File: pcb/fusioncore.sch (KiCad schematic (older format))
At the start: 114 parts, among them J1 Conn_02x12_Top_Bottom, J10 Pump_Misc_1, J11 Pump_Misc_2, J12 Flow_Warm, J13 Flow_Cold, J14 Trigger, J15 Valve_M2, J16 Valve_M3, J17 Valve_M4, J18 Conn_02x03_Top_Bottom, J19 Valve_Air_Lime, J2 Temperature, J20 Valve_Air_Rum, J21 Valve_Air_Out, J22 LED, J23 I2C_DBG, J3 40HAT, J4 Valve_M1, J5 WEIGHT, J6 Pump_Cold, J7 Pump_Warm, J8 Pump_Air, J9 CONN_01X02, Q1 DMG2305UX, Q12 AO3400A, Q13 AO3400A, Q14 AO3400A, Q16 MMBT4403, Q2 DMMT5401, Q3 AO3400A, Q4 AO3400A, Q5 AO3400A, Q6 AO3400A, Q7 AO3400A, SW1 POWER_ON, U1 HX711, U2 CAT24C32, U3 LTC2990, U4 LTC2990, U5 TXB0108DQSR

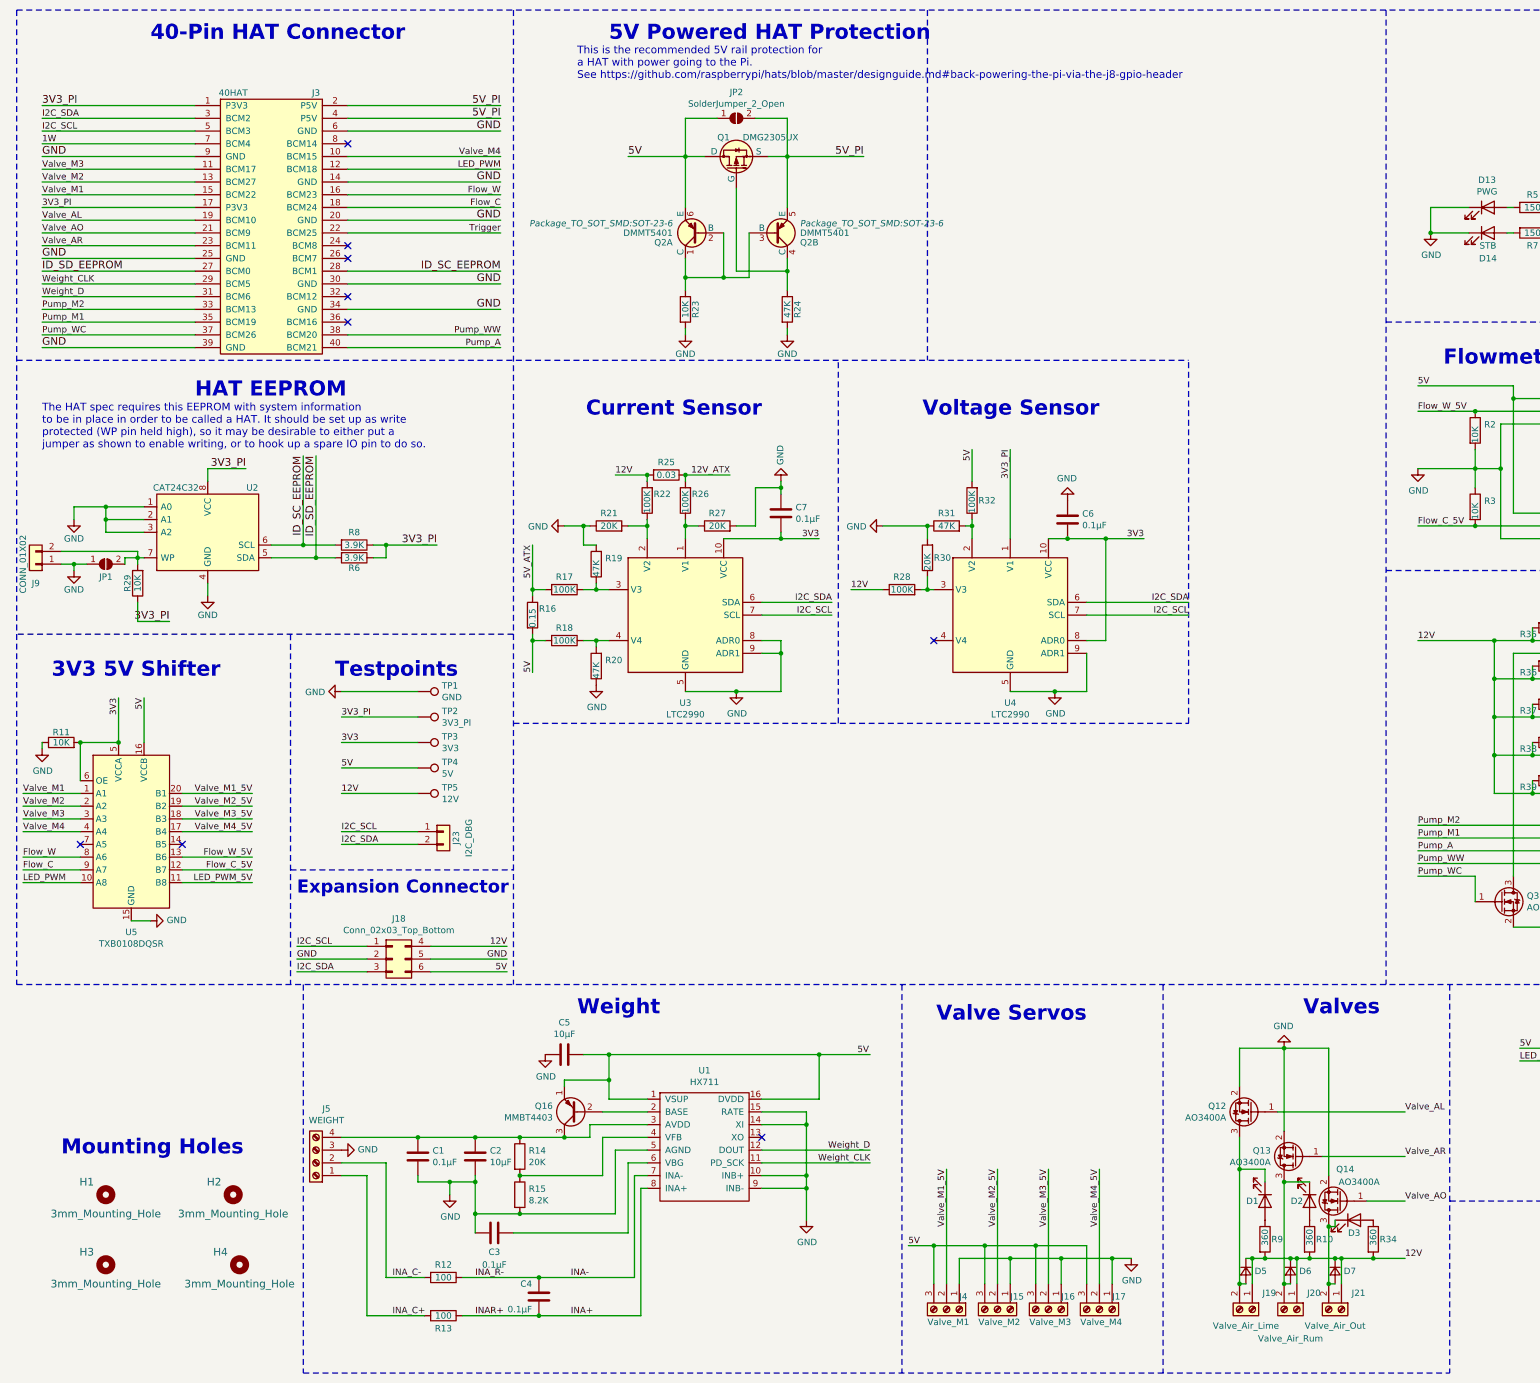
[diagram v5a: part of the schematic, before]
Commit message: Added JLC specific marker
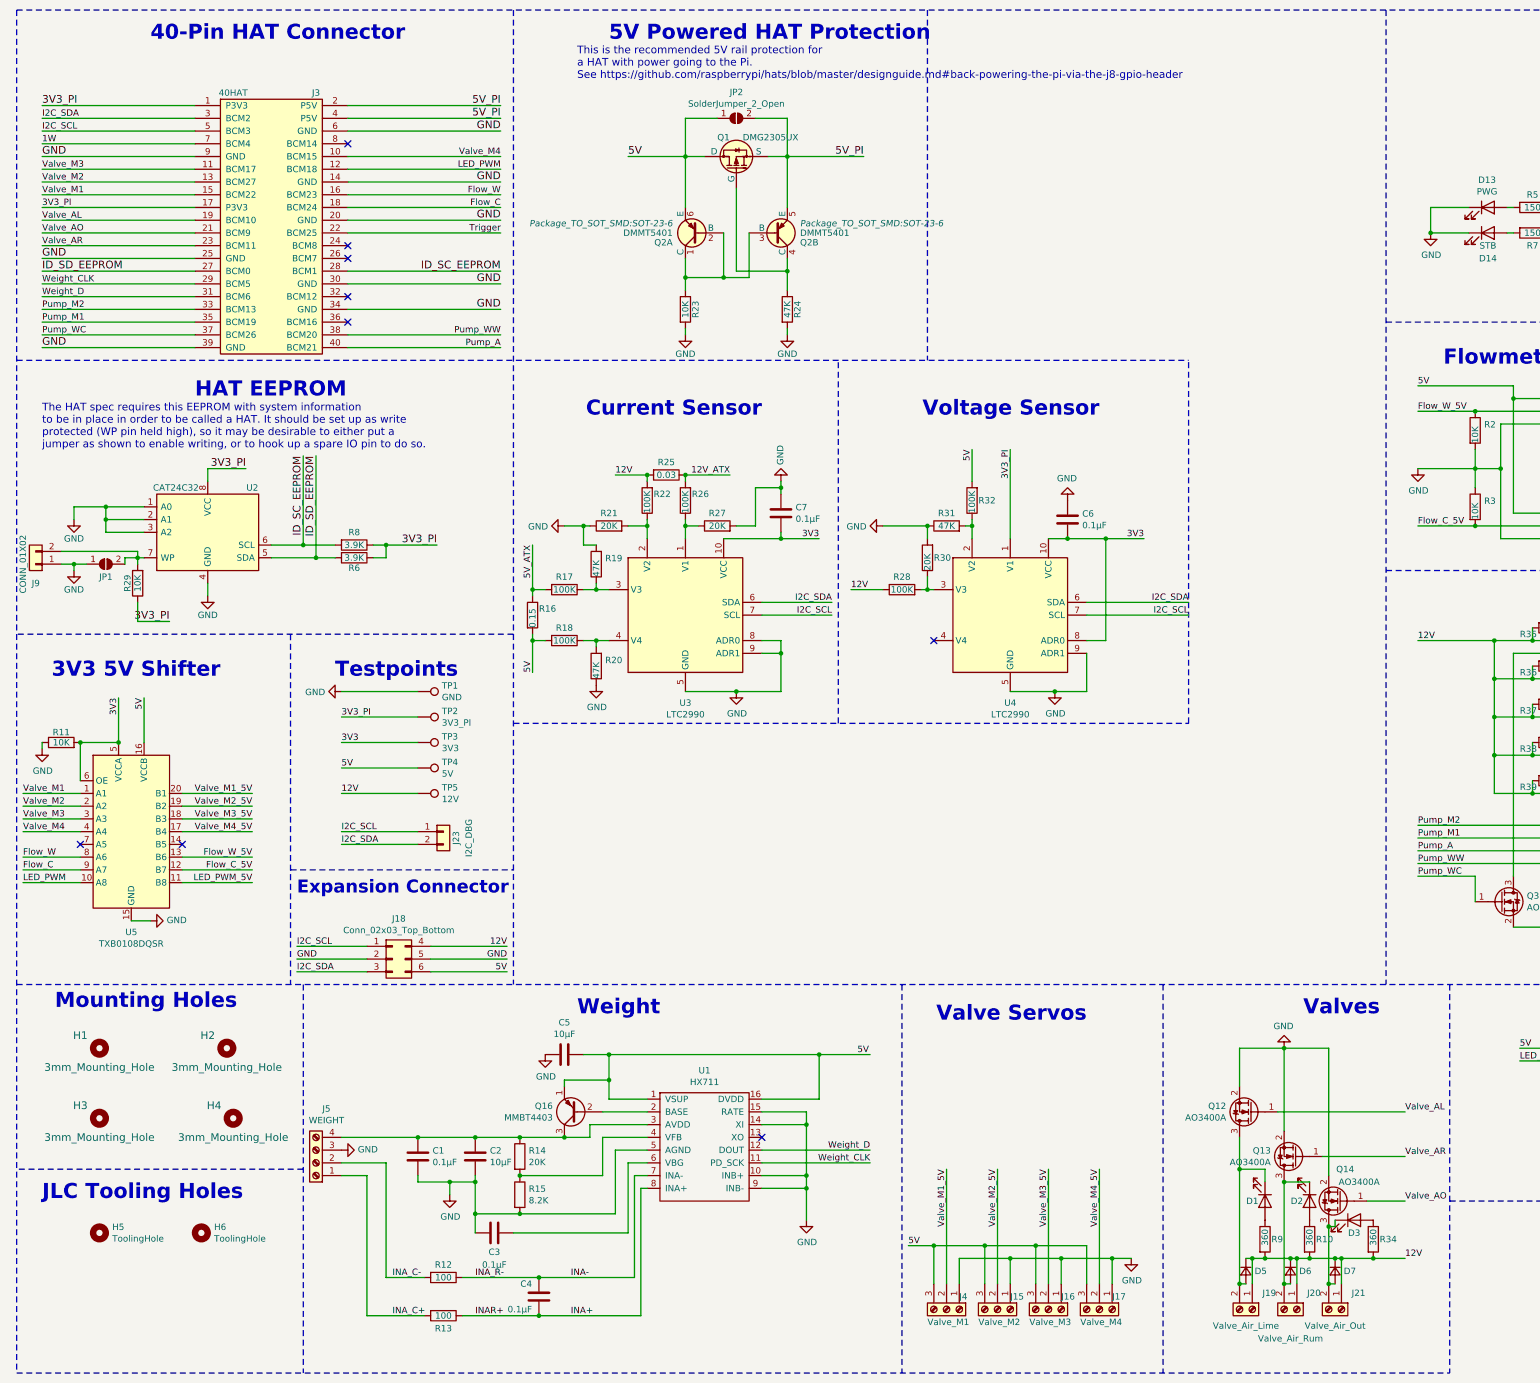
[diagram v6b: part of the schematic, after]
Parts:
- added H5, H6: ToolingHole, project_footprints:JLC_Tooling_Hole, symbol Mechanical:MountingHole
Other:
- note added: "JLC Tooling Holes"
- moved on the sheet: H1, H2, H3, H4
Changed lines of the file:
@@
 L Mechanical:MountingHole H1
 U 1 1 5834BC4A
-P 1200 9800
-F 0 "H1" H 1050 9900 60  0000 C CNN
-F 1 "3mm_Mounting_Hole" H 1200 9650 60  0000 C CNN
-F 2 "project_footprints:NPTH_3mm_ID" H 1100 9800 60  0001 C CNN
-F 3 "" H 1100 9800 60  0001 C CNN
-	1    1200 9800
+P 1150 8650
+F 0 "H1" H 1000 8750 60  0000 C CNN
+F 1 "3mm_Mounting_Hole" H 1150 8500 60  0000 C CNN
+F 2 "project_footprints:NPTH_3mm_ID" H 1050 8650 60  0001 C CNN
+F 3 "" H 1050 8650 60  0001 C CNN
+	1    1150 8650
 	1    0    0    -1
 $EndComp
@@
 L Mechanical:MountingHole H2
 U 1 1 5834BCDF
-P 2200 9800
-F 0 "H2" H 2050 9900 60  0000 C CNN
-F 1 "3mm_Mounting_Hole" H 2200 9650 60  0000 C CNN
-F 2 "project_footprints:NPTH_3mm_ID" H 2100 9800 60  0001 C CNN
-F 3 "" H 2100 9800 60  0001 C CNN
-	1    2200 9800
+P 2150 8650
+F 0 "H2" H 2000 8750 60  0000 C CNN
+F 1 "3mm_Mounting_Hole" H 2150 8500 60  0000 C CNN
+F 2 "project_footprints:NPTH_3mm_ID" H 2050 8650 60  0001 C CNN
+F 3 "" H 2050 8650 60  0001 C CNN
+	1    2150 8650
 	1    0    0    -1
 $EndComp
@@
 L Mechanical:MountingHole H3
 U 1 1 5834BD62
-P 1200 10350
-F 0 "H3" H 1050 10450 60  0000 C CNN
-F 1 "3mm_Mounting_Hole" H 1200 10200 60  0000 C CNN
-F 2 "project_footprints:NPTH_3mm_ID" H 1100 10350 60  0001 C CNN
-F 3 "" H 1100 10350 60  0001 C CNN
-	1    1200 10350
+P 1150 9200
+F 0 "H3" H 1000 9300 60  0000 C CNN
+F 1 "3mm_Mounting_Hole" H 1150 9050 60  0000 C CNN
+F 2 "project_footprints:NPTH_3mm_ID" H 1050 9200 60  0001 C CNN
+F 3 "" H 1050 9200 60  0001 C CNN
+	1    1150 9200
 	1    0    0    -1
 $EndComp
@@
 L Mechanical:MountingHole H4
 U 1 1 5834BDED
-P 2250 10350
-F 0 "H4" H 2100 10450 60  0000 C CNN
-F 1 "3mm_Mounting_Hole" H 2250 10200 60  0000 C CNN
-F 2 "project_footprints:NPTH_3mm_ID" H 2150 10350 60  0001 C CNN
-F 3 "" H 2150 10350 60  0001 C CNN
-	1    2250 10350
+P 2200 9200
+F 0 "H4" H 2050 9300 60  0000 C CNN
+F 1 "3mm_Mounting_Hole" H 2200 9050 60  0000 C CNN
+F 2 "project_footprints:NPTH_3mm_ID" H 2100 9200 60  0001 C CNN
+F 3 "" H 2100 9200 60  0001 C CNN
+	1    2200 9200
 	1    0    0    -1
 $EndComp
@@
 Text Notes 1900 3550 0    118  ~ 24
 HAT EEPROM
-Text Notes 850  9500 0    118  ~ 24
+Text Notes 800  8350 0    118  ~ 24
 Mounting Holes
 Text Notes 1550 750  0    118  ~ 24
@@
 	2750 8150 2750 11200
 Wire Notes Line
-	2750 11200 11750 11200
-Wire Notes Line
 	13650 2950 13650 4900
 Wire Notes Line
@@
 	500  8150 16050 8150
 Wire Notes Line
-	500  500  500  8150
-Wire Notes Line
 	500  500  16050 500
 Text Notes 9000 3700 2    118  ~ 24
@@
 Text Label 3050 7050 0    50   ~ 0
 I2C_SDA
+Wire Notes Line
+	500  11200 11750 11200
+Wire Notes Line
+	500  500  500  11200
+Wire Notes Line
+	2750 9600 500  9600
+Text Notes 700  9850 0    118  ~ 24
+JLC Tooling Holes
+$Comp
+L Mechanical:MountingHole H5
+U 1 1 5E48D44C
+P 1150 10100
+F 0 "H5" H 1250 10146 50  0000 L CNN
+F 1 "ToolingHole" H 1250 10055 50  0000 L CNN
+F 2 "project_footprints:JLC_Tooling_Hole" H 1150 10100 50  0001 C CNN
+F 3 "~" H 1150 10100 50  0001 C CNN
+	1    1150 10100
+	1    0    0    -1
+$EndComp
+$Comp
+L Mechanical:MountingHole H6
+U 1 1 5E48DB8E
+P 1950 10100
+F 0 "H6" H 2050 10146 50  0000 L CNN
+F 1 "ToolingHole" H 2050 10055 50  0000 L CNN
+F 2 "project_footprints:JLC_Tooling_Hole" H 1950 10100 50  0001 C CNN
+F 3 "~" H 1950 10100 50  0001 C CNN
+	1    1950 10100
+	1    0    0    -1
+$EndComp
 $EndSCHEMATC

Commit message: Fix J23
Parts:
- J23: footprint Connector_PinHeader_2.54mm:PinHeader_1x02_P2.54mm_Vertical -> Connector_PinHeader_2.54mm:PinHeader_1x04_P2.54mm_Vertical; symbol Connector_Generic:Conn_01x02 -> Connector_Generic:Conn_01x04
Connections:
- net 3V3: now also J23.1 (Pin_1)
- net GND: now also J23.4 (Pin_4)
- net I2C_SCL: now also J23.2 (Pin_2); no longer J23.1 (Pin_1)
- net I2C_SDA: now also J23.3 (Pin_3); no longer J23.2 (Pin_2)
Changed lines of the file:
@@
 	3750 7850 4350 7850
 $Comp
-L Connector_Generic:Conn_01x02 J23
+L Connector_Generic:Conn_01x04 J23
 U 1 1 5E8D6410
 P 3850 6950
 F 0 "J23" V 3950 6900 50  0000 C CNN
 F 1 "I2C_DBG" V 4050 6900 50  0000 C CNN
-F 2 "Connector_PinHeader_2.54mm:PinHeader_1x02_P2.54mm_Vertical" H 3850 6950 50  0001 C CNN
+F 2 "Connector_PinHeader_2.54mm:PinHeader_1x04_P2.54mm_Vertical" H 3850 6950 50  0001 C CNN
 F 3 "" H 3850 6950 50  0000 C CNN
 	1    3850 6950
@@
 	1    0    0    -1
 $EndComp
+Wire Wire Line
+	3650 6850 3050 6850
+Wire Wire Line
+	3650 7150 3050 7150
+Text Label 3050 6850 0    50   ~ 0
+3V3
+Text Label 3050 7150 0    50   ~ 0
+GND
 $EndSCHEMATC

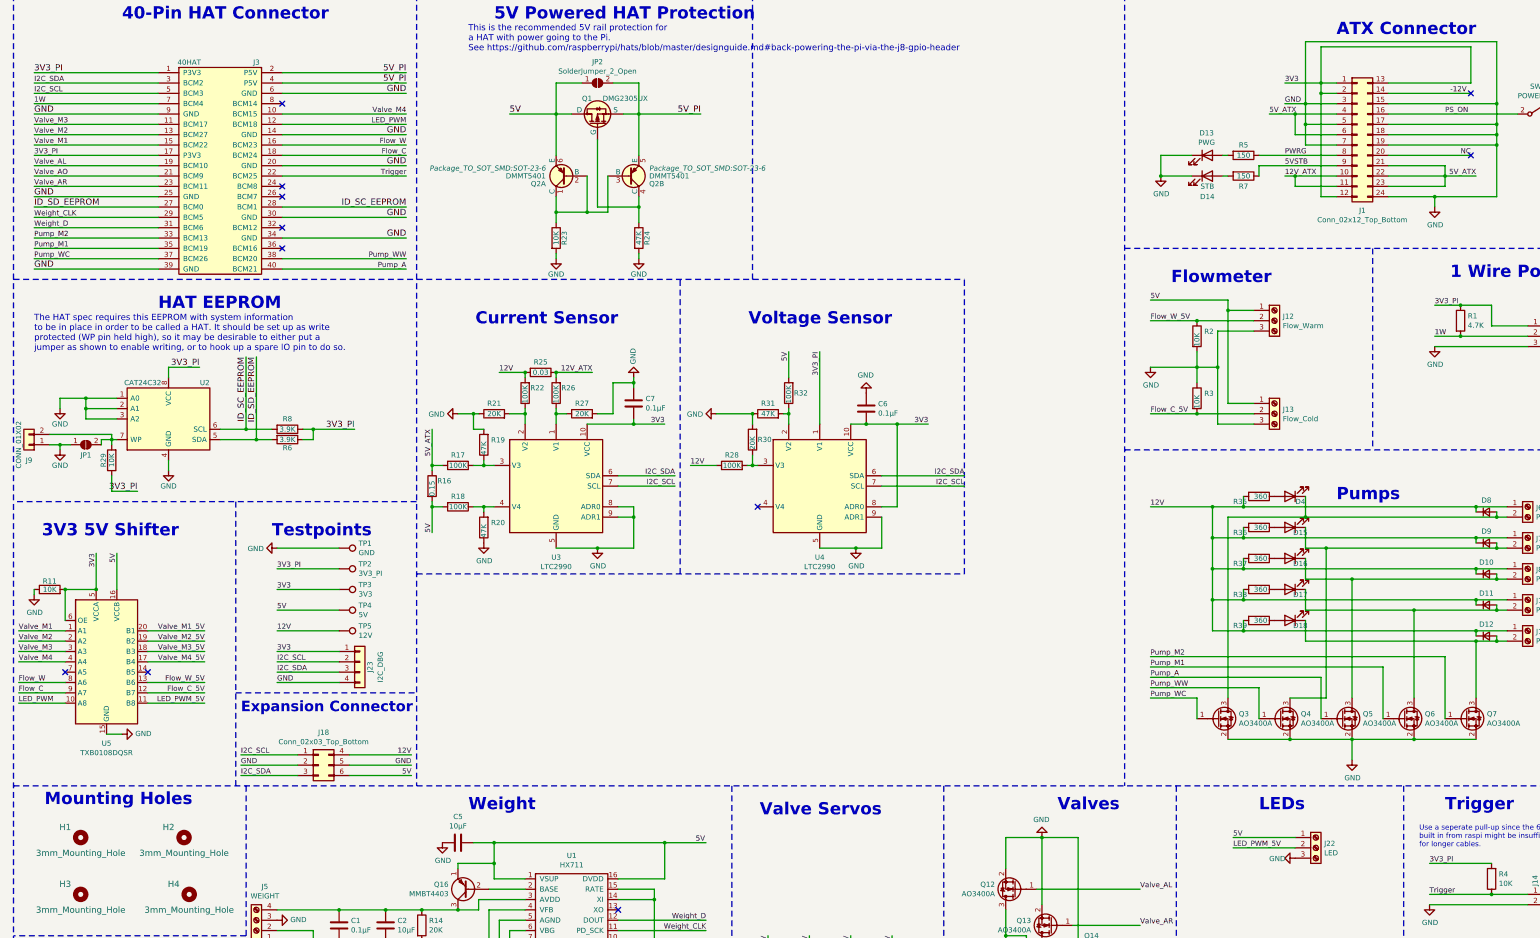
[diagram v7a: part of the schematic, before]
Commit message: Replaced LTC2990 with INA226 in schema
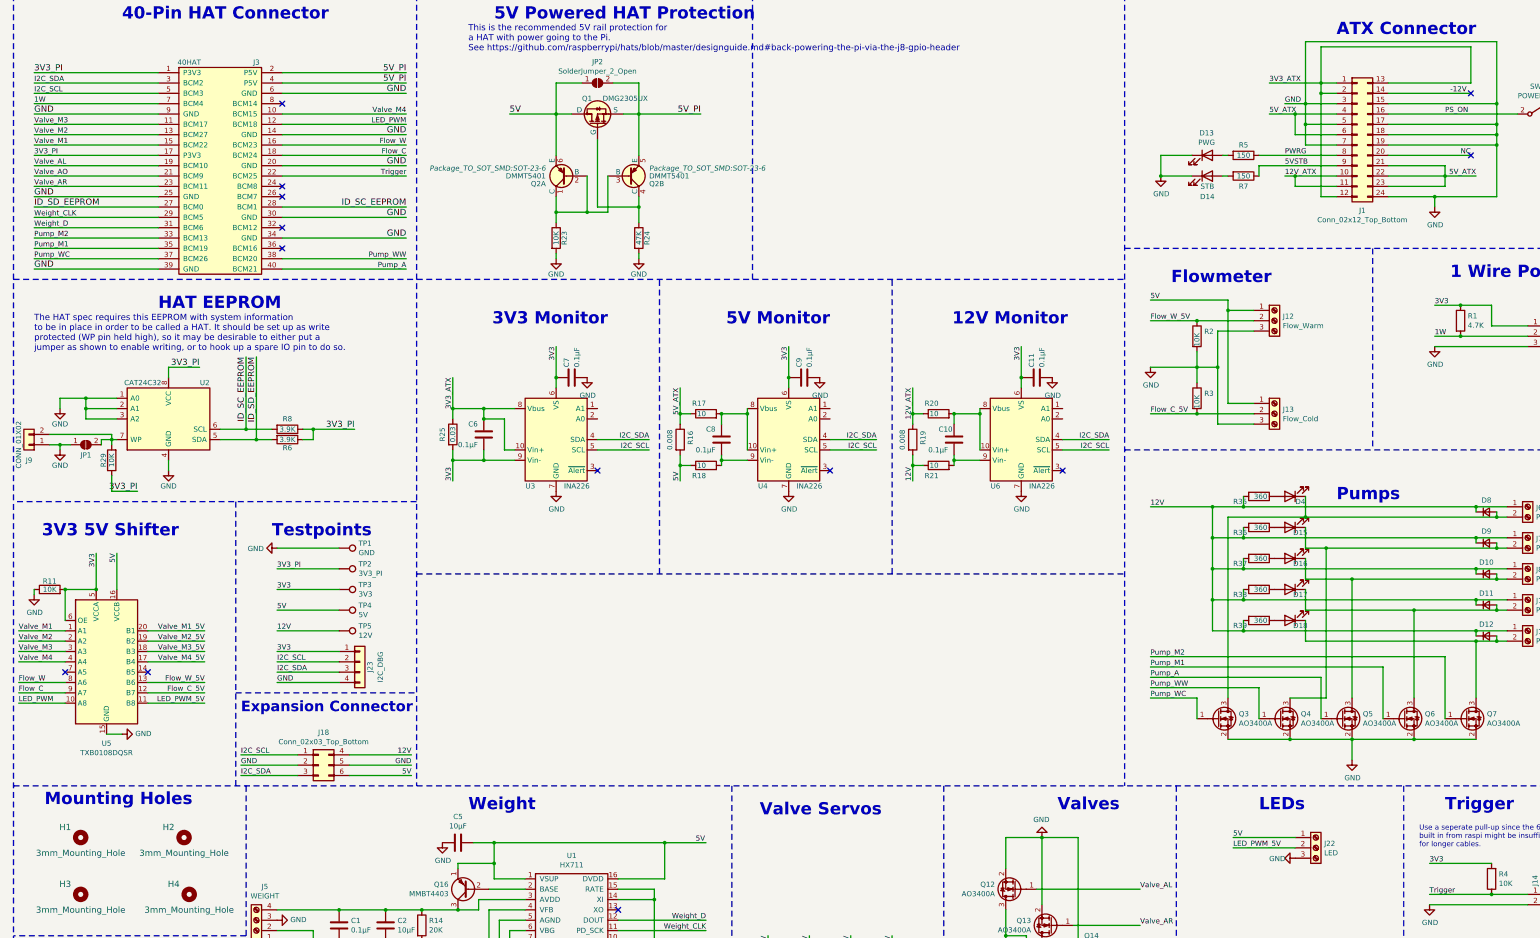
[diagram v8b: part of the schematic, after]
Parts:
- removed R22, R26, R28, R32: 100K, Resistor_SMD:R_0805_2012Metric_Pad1.15x1.40mm_HandSolder, symbol Device:R
- removed R27, R30: 20K, Resistor_SMD:R_0805_2012Metric_Pad1.15x1.40mm_HandSolder, symbol Device:R
- removed R31: 47K, Resistor_SMD:R_0805_2012Metric_Pad1.15x1.40mm_HandSolder, symbol Device:R
- removed U3, U4: LTC2990, Package_SO:MSOP-10_3x3mm_P0.5mm, symbol Sensor:LTC2990
- added C10, C11, C8, C9: 0.1μF, Capacitor_SMD:C_0805_2012Metric_Pad1.15x1.40mm_HandSolder, symbol Device:C
- added U3, U4, U6: INA226, Package_SO:VSSOP-10_3x3mm_P0.5mm, symbol Analog_ADC:INA226
- R16: value 0.15 -> 0.008; footprint Resistor_SMD:R_1206_3216Metric_Pad1.42x1.75mm_HandSolder -> Resistor_SMD:R_2512_6332Metric_Pad1.52x3.35mm_HandSolder; LCSC C247454 -> C76241
- R17, R18: value 100K -> 10; LCSC C17407 -> C17415
- R19: value 47K -> 0.008; footprint Resistor_SMD:R_0805_2012Metric_Pad1.15x1.40mm_HandSolder -> Resistor_SMD:R_2512_6332Metric_Pad1.52x3.35mm_HandSolder; LCSC C17713 -> C76241
- R20: value 47K -> 10; LCSC C17713 -> C17415
- R21: value 20K -> 10; LCSC C4328 -> C17415
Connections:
- net 12V: now also R19.2, R21.1; no longer R25.2
- net 12V_ATX: now also R19.1, R20.1; no longer R25.1
- net 3V3: now also C6.1, J2.1 (Pin_1), R1.1, R25.2, R4.2, C11.2, C9.2, U3.6 (VS), U3.9 (Vin-), U4.6 (VS), U6.6 (VS); no longer C6.2, J1.1 (Pin_1), J1.12 (Pin_12), J1.13 (Pin_13), J1.2 (Pin_2)
- net 3V3_PI: no longer J2.1 (Pin_1), R1.1, R4.2
- net 5V: now also R18.1; no longer R18.2
- net 5V_ATX: now also R17.1; no longer R17.2
- net GND: now also C11.1, C9.1, U3.7 (GND), U4.7 (GND), U6.7 (GND); no longer C6.1, R19.2, R20.1, R21.1
- net I2C_SCL: now also U3.5 (SCL), U4.5 (SCL), U6.5 (SCL)
- net I2C_SDA: now also U3.4 (SDA), U4.4 (SDA), U6.4 (SDA)
- net at R21.2: now also C10.1, U6.9 (Vin-)
- net at R20.2: now also C10.2, U6.10 (Vin+), U6.8 (Vbus); no longer R18.1
- new net: C8.2, R17.2, U4.10 (Vin+), U4.8 (Vbus)
- new net: C8.1, R18.2, U4.9 (Vin-)
- new net 3V3_ATX: C6.2, J1.1 (Pin_1), J1.12 (Pin_12), J1.13 (Pin_13), J1.2 (Pin_2), R25.1, U3.10 (Vin+), U3.8 (Vbus)
- no-connect marks 11 -> 13
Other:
- note added: "12V Monitor"
- note added: "3V3 Monitor"
- note added: "5V Monitor"
- note removed: "Current Sensor"
- note removed: "Voltage Sensor"
- moved on the sheet: R16, R25
